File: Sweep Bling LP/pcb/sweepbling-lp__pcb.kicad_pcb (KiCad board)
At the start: 2 copper layers, 216.9 x 86.9 mm, 54 parts, among them SW1 SW_Push, SW10 SW_Push, SW10_r1 SW_Push, SW11 SW_Push, SW11_r1 SW_Push, SW12 SW_Push, SW12_r1 SW_Push, SW13 SW_Push, SW13_r1 SW_Push, SW14 SW_Push, SW14_r1 SW_Push, SW15 SW_Push, SW15_r1 SW_Push, SW16 SW_Push, SW16_r1 SW_Push, SW17 SW_Push, SW17_r1 SW_Push, SW1_r1 SW_Push, SW2 SW_Push, SW2_r1 SW_Push, SW3 SW_Push, SW3_r1 SW_Push, SW4 SW_Push, SW4_r1 SW_Push, SW5 SW_Push, SW5_r1 SW_Push, SW6 SW_Push, SW6_r1 SW_Push, SW7 SW_Push, SW7_r1 SW_Push, SW8 SW_Push, SW8_r1 SW_Push, SW9 SW_Push, SW9_r1 SW_Push, U1 ProMicro-kbd, U2 ProMicro-kbd

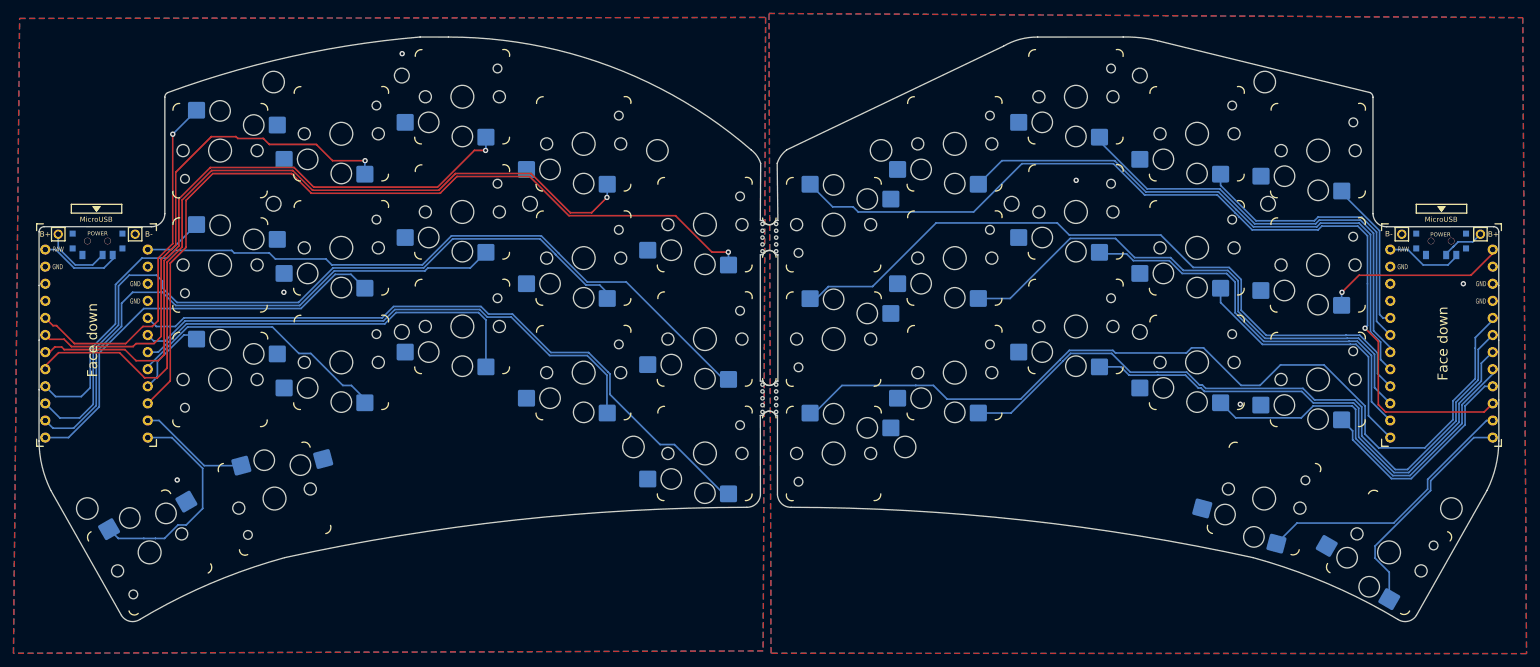
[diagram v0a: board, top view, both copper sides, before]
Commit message: redo edge cuts and mirror
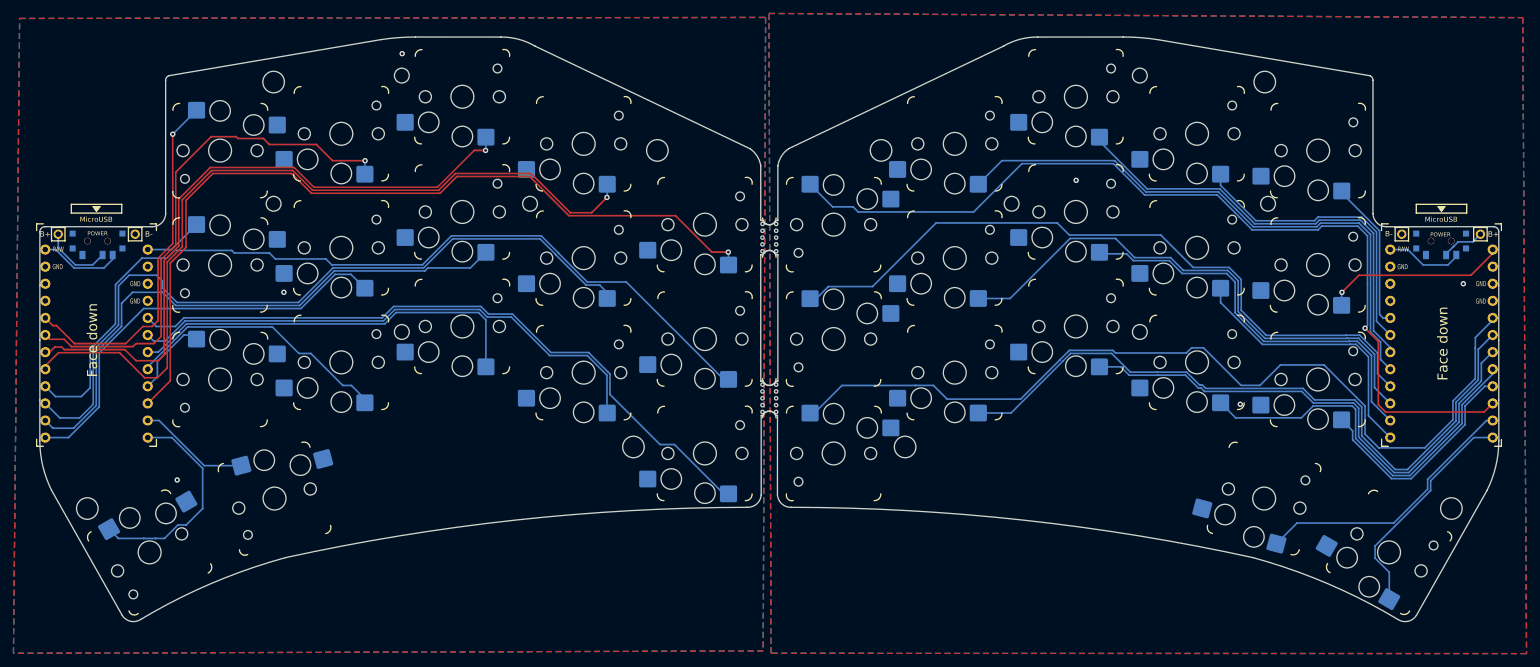
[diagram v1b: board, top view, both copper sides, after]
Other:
- board size 216.9 x 86.9 mm -> 216.8 x 86.9 mm
